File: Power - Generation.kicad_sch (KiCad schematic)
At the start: 0 parts

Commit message: [01/07/2026][MCU - IOs] Update
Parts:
- added U3: TPSM63603RDHR, Duc_Library:QFN-30_L6.0-W4.0-P0.50_TLVM13630RDHR, symbol Duc_Library:TPSM63603RDHR
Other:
- company: (none) -> ${COMPANY}
- title: (none) -> Power - Generation
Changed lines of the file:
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@@
 	(generator "eeschema")
 	(generator_version "9.0")
-	(paper "A4")
+	(paper "A3")
+	(title_block
+		(title "Power - Generation")
+		(date "2026-06-27")
+		(rev "${REVISION}")
+		(company "${COMPANY}")
+	)
+	(text_box "[${#}] ${TITLE}"
+		(exclude_from_sim no)
+		(at 149.86 15.24 0)
+		(size 128.27 12.7)
+		(margins 5.9999 5.9999 5.9999 5.9999)
+		(stroke
+			(width -0.0001)
+			(type default)
+		)
+		(fill
+			(type none)
+		)
+		(effects
+			(font
+				(face "Times New Roman")
+				(size 8 8)
+				(thickness 1.2)
+				(bold yes)
+				(color 162 22 34 1)
+			)
+		)
+	)
+	(symbol
+		(lib_id "Duc_Library:TPSM63603RDHR")
+		(at 114.3 105.41 0)
+		(unit 1)
+		(exclude_from_sim no)
+		(in_bom yes)
+		(on_board yes)
+		(dnp no)
+		(fields_autoplaced yes)
+		(property "Reference" "U3"
+			(at 114.3 72.39 0)
+			(effects
+				(font
+					(size 1.27 1.27)
+				)
+			)
+		)
+		(property "Value" "TPSM63603RDHR"
+			(at 114.3 74.93 0)
+			(effects
+				(font
+					(size 1.27 1.27)
+				)
+			)
+		)
+		(property "Footprint" "Duc_Library:QFN-30_L6.0-W4.0-P0.50_TLVM13630RDHR"
+			(at 114.3 138.43 0)
+			(effects
+				(font
+					(size 1.27 1.27)
+				)
+				(hide yes)
+			)
+		)
+		(property "Datasheet" "https://www.lcsc.com/datasheet/C5219327.pdf"
+			(at 114.3 140.97 0)
+			(effects
+				(font
+					(size 1.27 1.27)
+				)
+				(hide yes)
+			)
+		)
+		(property "Description" ""
+			(at 114.3 105.41 0)
+			(effects
+				(font
+					(size 1.27 1.27)
+				)
+				(hide yes)
+			)
+		)
+		(property "Manufacturer" "TI(德州仪器)"
+			(at 114.3 143.51 0)
+			(effects
+				(font
+					(size 1.27 1.27)
+				)
+				(hide yes)
+			)
+		)
+		(property "MPN" "TPSM63603RDHR"
+			(at 114.3 146.05 0)
+			(effects
+				(font
+					(size 1.27 1.27)
+				)
+				(hide yes)
+			)
+		)
+		(property "LCSC Part" "C5219327"
+			(at 114.3 148.59 0)
+			(effects
+				(font
+					(size 1.27 1.27)
+				)
+				(hide yes)
+			)
+		)
+		(pin "24"
+		)
+		(pin "7"
+		)
+		(pin "13"
+		)
+		(pin "14"
+		)
+		(pin "28"
+		)
+		(pin "10"
+		)
+		(pin "23"
+		)
+		(pin "30"
+		)
+		(pin "26"
+		)
+		(pin "20"
+		)
+		(pin "6"
+		)
+		(pin "25"
+		)
+		(pin "12"
+		)
+		(pin "9"
+		)
+		(pin "8"
+		)
+		(pin "19"
+		)
+		(pin "3"
+		)
+		(pin "29"
+		)
+		(pin "18"
+		)
+		(pin "2"
+		)
+		(pin "15"
+		)
+		(pin "11"
+		)
+		(pin "16"
+		)
+		(pin "27"
+		)
+		(pin "22"
+		)
+		(pin "17"
+		)
+		(pin "4"
+		)
+		(pin "5"
+		)
+		(pin "21"
+		)
+		(pin "1"
+		)
+		(instances
+			(project "Master_Hand_Kicad"
+				(path "/f9e05184-c88b-4a88-ae9c-ab2bdb32be7c/c5103ceb-5325-4a84-a025-9638a412984e/042ebd96-5d8b-461b-acb5-c7c1300dab56"
+					(reference "U3")
+					(unit 1)
+				)
+			)
+		)
+	)
 )

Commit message: [07/07/2026][Power - Generation] Update
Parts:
- removed U3: TPSM63603RDHR, Duc_Library:QFN-30_L6.0-W4.0-P0.50_TLVM13630RDHR, symbol Duc_Library:TPSM63603RDHR
- added C19, C20, C22, C23, C24, C29, C30: CAP CER 1206, Duc_Library:C1206, symbol Duc-Capacitors:CAP CER 1206
- added C21, C25, C26, C27, C28: CAP CER 0402, Duc_Library:C0402, symbol Duc-Capacitors:CAP CER 0402
- added FB3, FB4: 1k @ 100MHz, Duc_Library:L0805, symbol Duc-Inductors:PBBHAQ2012H-102T10
- added L1: ANR3015T2R2M, Duc:IND-SMD_L3.0-W3.0_SMNR3015, symbol Duc-Inductors:ANR3015T2R2M
- added R1, R2, R3, R4, R5: RES 0402, Duc_Library:R0402, symbol Duc-Resistors:RES SMD 0402
- added R6: RES 0.1% 0603, Duc:R0603, symbol Duc-Resistors:RES SMD 0603
- added U3: TPSM63603RDHR, Duc_Library:QFN-30_L6.0-W4.0-P0.50_TLVM13630RDHR, symbol Duc-Power:TPSM63603RDHR
- added U4: TPS62162DSG, Duc:WSON-8_L2.0-W2.0-P0.50-TL-EP, symbol Duc-Power:TPS62162DSG
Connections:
- new net: L1.1, U4.7 (SW)
- new net: R5.2, U3.1 (RT)
- new net: C19.2, C20.2, C26.2, C30.2, FB3., R1.2, U3.18 (VIN), U3.19 (VIN), U3.3 (VIN), U3.4 (VIN)
- new net: C21.2, U3.23 (VCC)
- new net: C28.2, C29.2, FB4., U4.2 (VIN)
- new net: C24.1, U4.5 (FB)
- new net: R6.1, U4.8 (PG)
- new net: U3.20 (CBOOT), U3.21 (RBOOT)
- new net +3V3: C24.2, L1.2, R6.2, U4.6 (VOS)
- new net +5V: C22.2, C23.2, C27.2, FB4., R3.2, U3.10 (VOUT), U3.12 (VOUT), U3.13 (VOUT), U3.14 (VOUT), U3.15 (VOUT), U3.22 (VLDOIN), U3.30 (VOUT), U3.7 (VOUT), U3.8 (VOUT), U3.9 (VOUT)
- new net +VBAT: C25.2, FB3.
- new net AGND: R4.1, U3.24 (AGND), U3.27 (AGND), U4.4 (AGND)
- new net EN_3V3: U3.26 (PG), U4.3 (EN)
- new net EN_5V: R1.1, R2.2, U3.2 (EN/SYNC)
- new net FB_5V: R3.1, R4.2, U3.25 (FB)
- new net GND: C19.1, C20.1, C21.1, C22.1, C23.1, C25.1, C26.1, C27.1, C28.1, C29.1, C30.1, R2.1, R5.1, U3.16 (PGND), U3.17 (PGND), U3.28 (PGND), U3.29 (PGND), U3.5 (PGND), U3.6 (PGND), U4.1 (PGND)
- no-connect marks 0 -> 2

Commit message: Update Power Generation Schematic
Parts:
- added C31, C32: 1uF 10V 1206, Duc_Library:C1206, symbol Duc-Capacitors:CAP CER 1206
- added C33: 25SVPF330M, Duc:CAP-SMD_BD10.0-L10.3-W10.3-LS11.0-FD, symbol Duc-Capacitors:25SVPF330M
- added C34, C35, C36, C37, C38, C39, C40, C41, C42, C43: 10uF 35V 0603, Duc:C0603, symbol Duc-Capacitors:CAP CER 0603
- added D1: SS34, Duc:SMA_L4.3-W2.5-LS5.0-RD, symbol Duc-Diodes:SS34
- added U5: TLV75533PDBVR, Duc:SOT-23-5_L3.0-W1.7-P0.95-LS2.8-BR, symbol Duc-Power:TLV75533PDBVR
- C19, C20: value CAP CER 1206 -> 4.7uF 100V 1206
- C21: value CAP CER 0402 -> 1uF 25V 0402
- C22, C29: value CAP CER 1206 -> 10uF 25V 1206
- C23: value CAP CER 1206 -> 100nF 25V 1206
- C24: value CAP CER 1206 -> 22uF 10V 1206
- C25, C26, C27, C28: value CAP CER 0402 -> 2.2uF 100V 0402
- C30: value CAP CER 1206 -> 10uF 100V 1206
- R1: value RES 0402 -> 40.2K 0.1% 0402
- R2, R4: value RES 0402 -> 10K 0.1% 0402
- R3: value RES 0402 -> 41.2K 0.1% 0402
- R5: value RES 0402 -> 13K 0.1% 0402
- R6: value RES 0.1% 0603 -> 100K 0.1% 0603
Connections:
- net +5V: now also R1.2, C31.2, U5.1 (IN); no longer R3.2
- net +VBAT: now also C33.1, C34.1, C35.1, C36.1, C37.1, C38.1, C39.1, C40.1, C41.1, C42.1, C43.1, D1.2 (A); no longer C25.2, FB3.
- net AGND: now also R2.1; no longer R4.1
- net EN_3V3: now also U5.3 (EN)
- net EN_5V: now also R3.1, R4.2; no longer R1.1, R2.2
- net FB_5V: now also R1.1, R2.2; no longer R3.1, R4.2
- net GND: now also R4.1, C31.1, C32.1, C33.2, C34.2, C35.2, C36.2, C37.2, C38.2, C39.2, C40.2, C41.2, C42.2, C43.2, U5.2 (GND); no longer R2.1
- net F_VIN_5V: now reaches C19.2, C20.2, C26.2, C30.2, FB3., U3.18 (VIN), U3.19 (VIN), U3.3 (VIN), U3.4 (VIN)
- net F_VIN_5V: now also R3.2; no longer R1.2
- net F_VIN_3V3: now reaches C28.2, C29.2, FB4., U4.2 (VIN)
- new net: C25.2, D1.1 (C), FB3.
- new net +A3V3: C32.2, U5.5 (OUT)
- no-connect marks 2 -> 3
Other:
- moved on the sheet: C19, C20, C21, C22, C23, C24, C25, C26, C27, C28, C29, C30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

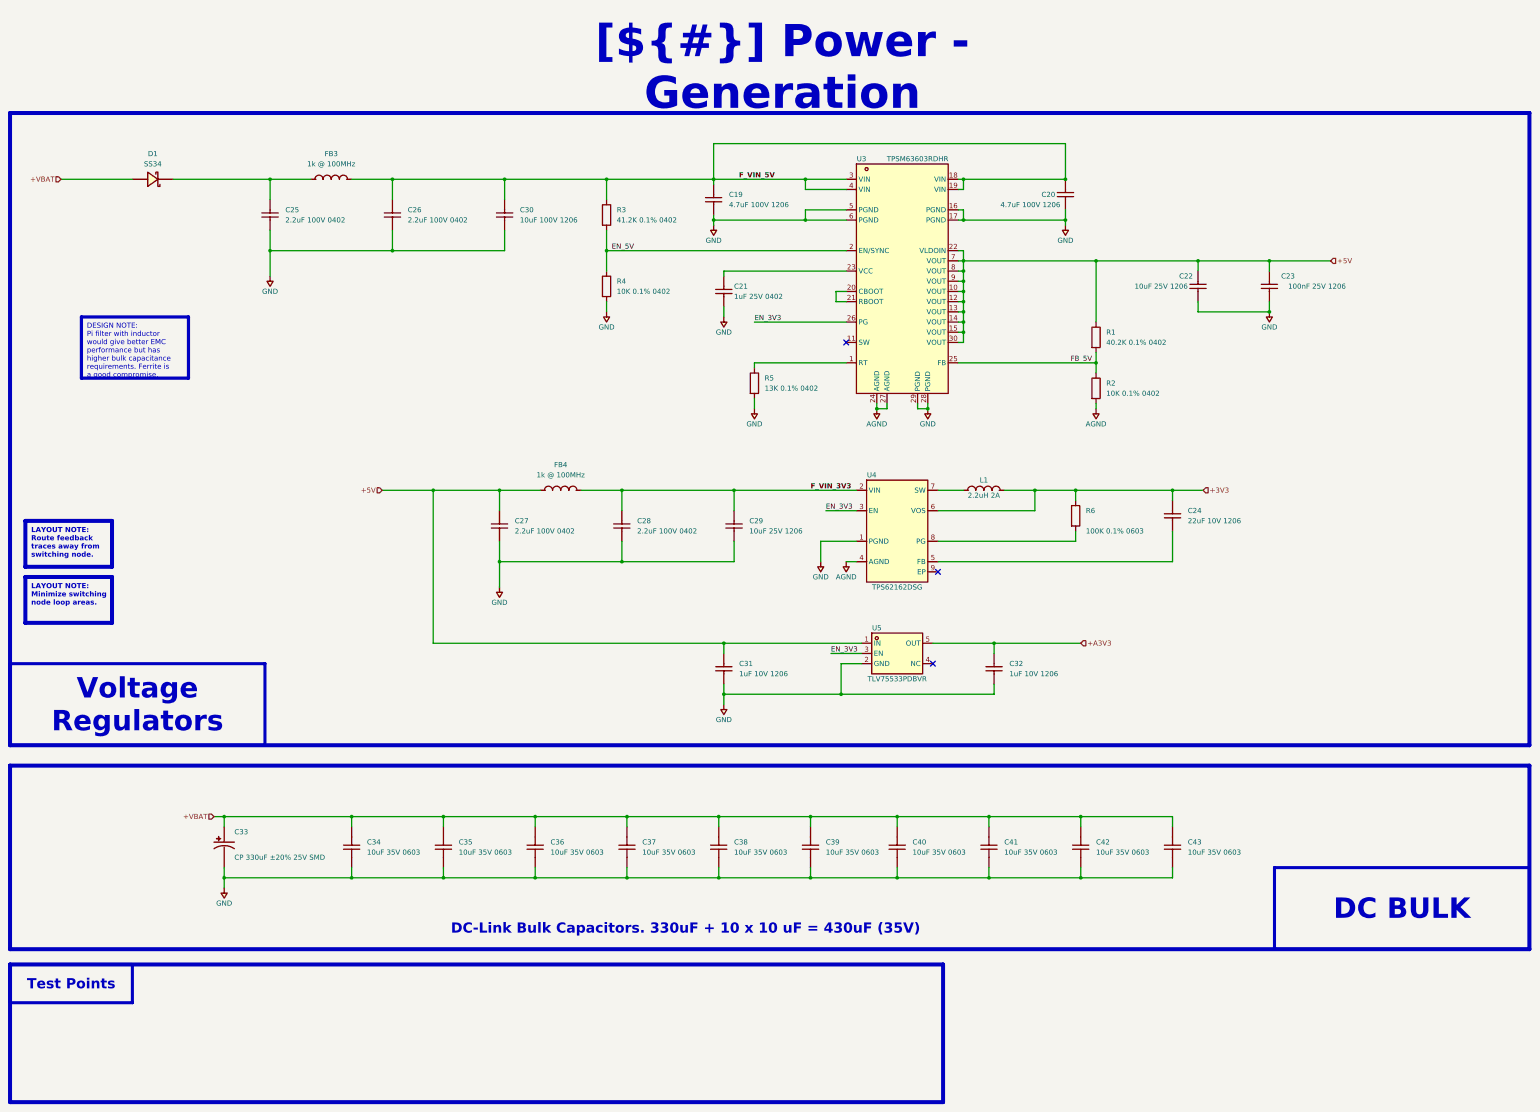
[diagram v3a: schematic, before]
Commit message: Update Power Connector & Motor Control Schematic
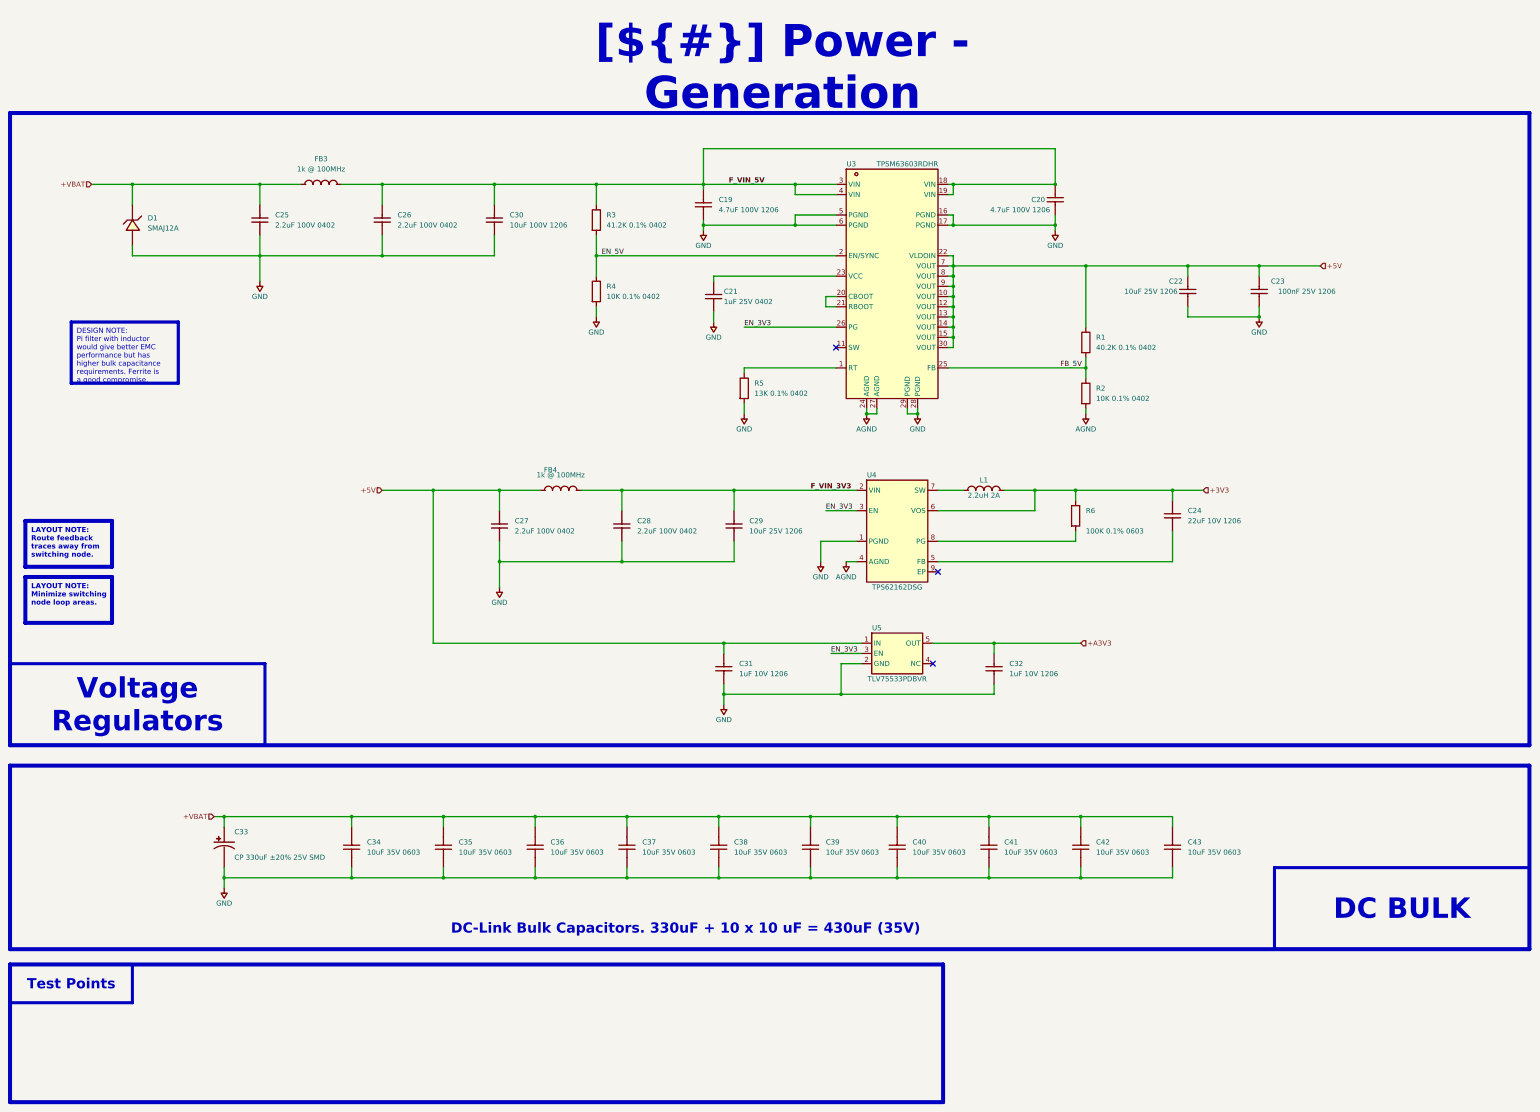
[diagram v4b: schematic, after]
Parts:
- removed D1: SS34, Duc:SMA_L4.3-W2.5-LS5.0-RD, symbol Duc-Diodes:SS34
- added D1: SMAJ12A, Duc:SMA_L4.3-W2.6-LS5.2-RD, symbol Duc-Diodes:SMAJ12A
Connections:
- net +VBAT: now also C25.2, FB3., D1.1 (C)
- net GND: now also D1.2 (A)
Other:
- moved on the sheet: C19, C20, C21, C22, C23, C25, C26, C30, FB3, R1, R2, R3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

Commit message: Update Schematic
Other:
- title: Power - Generation -> (none)
